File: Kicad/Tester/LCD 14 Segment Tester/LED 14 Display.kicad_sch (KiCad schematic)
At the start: 14 parts, among them IC4 SST39VF010-70-4I-WHE, IC5 SN74ABT245BDBR, IC8 SST39VF010-70-4I-WHE, IC9 SN74ABT245BDBR

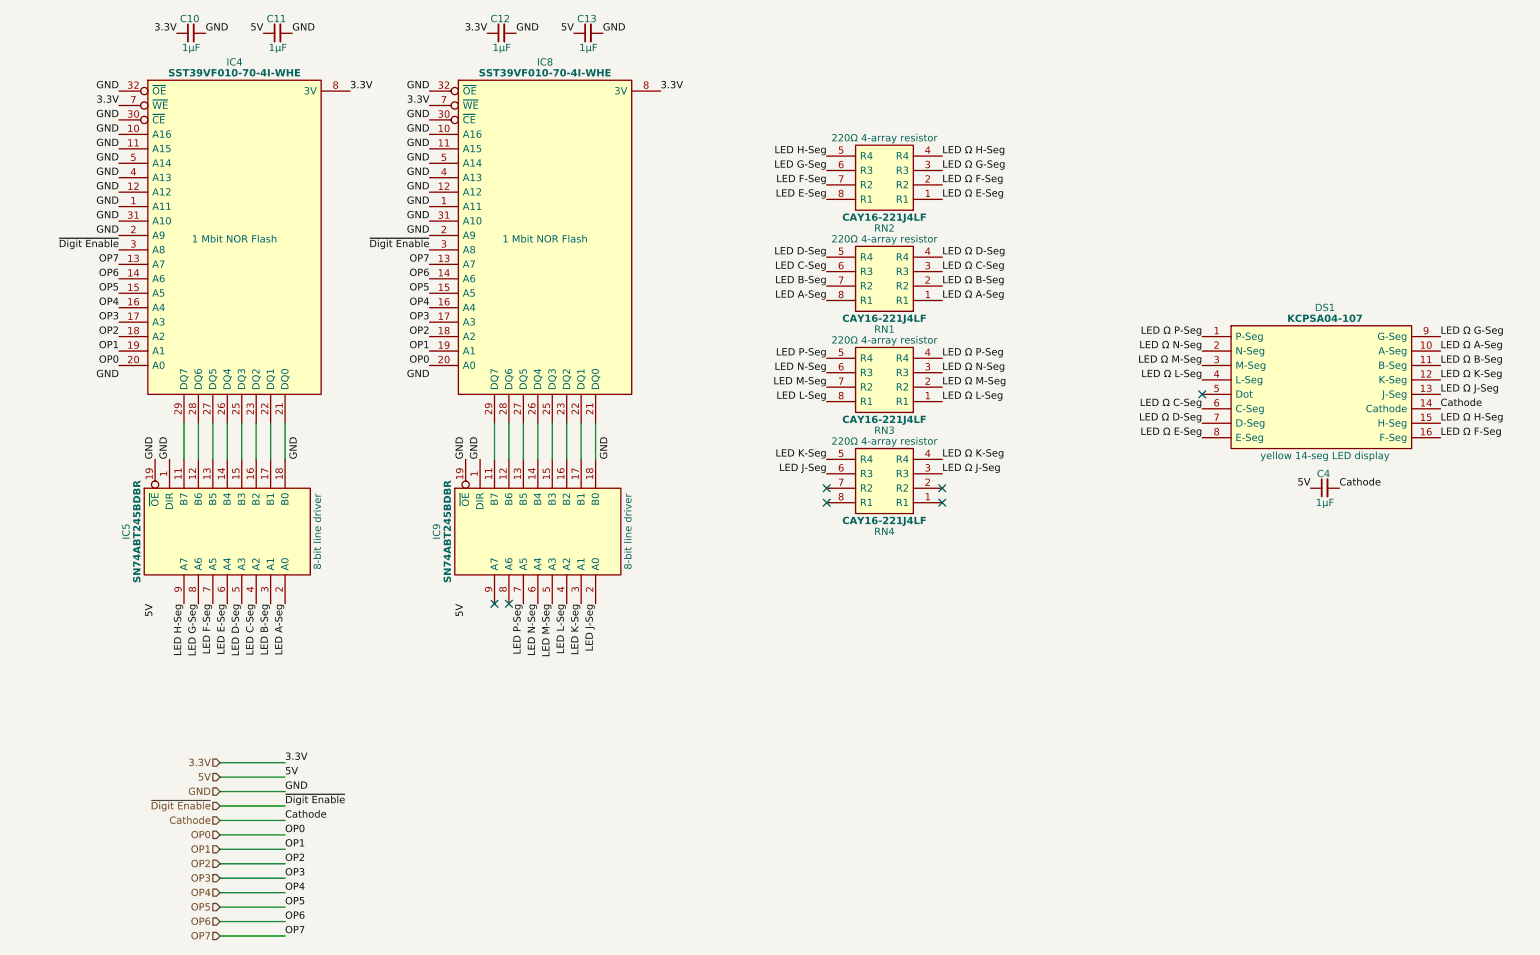
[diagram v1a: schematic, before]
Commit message: Laid out LCD 14 Segment tester PCB.
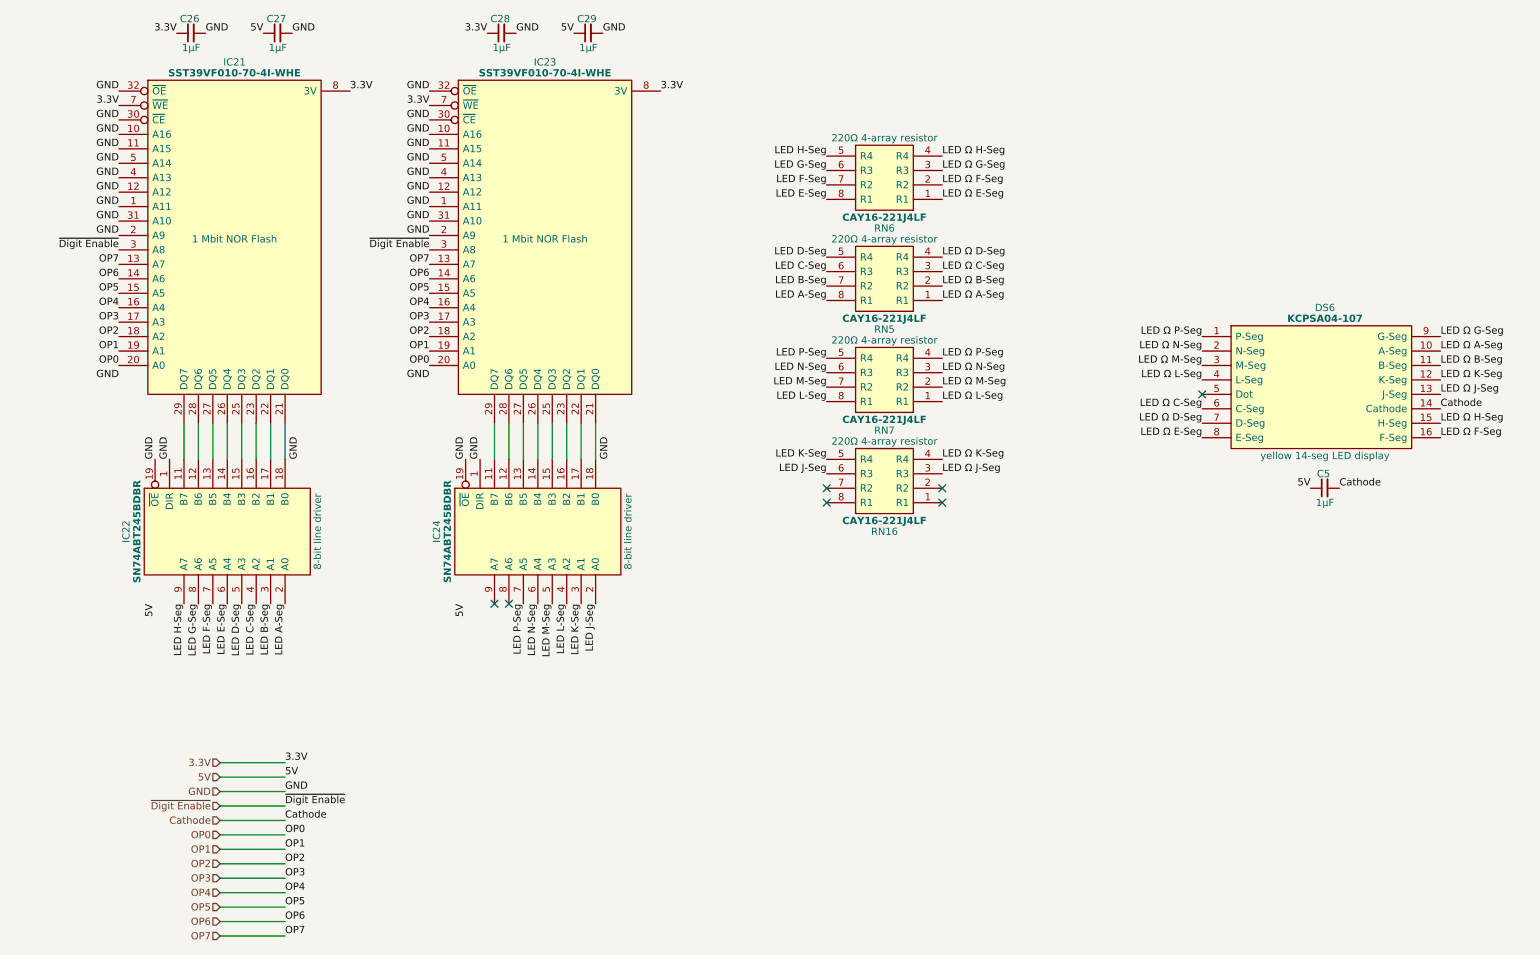
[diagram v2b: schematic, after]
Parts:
- IC21: renamed from IC4; footprint SamacSys_Parts:SOP50P1400X120-32N -> SamacSys_Parts:DIP-32_TSSOP_14mm_Adapter
- IC23: renamed from IC8; footprint SamacSys_Parts:SOP50P1400X120-32N -> SamacSys_Parts:DIP-32_TSSOP_14mm_Adapter
- renumbered C10 to C26, C11 to C27, C12 to C28, C13 to C29, C4 to C5, DS1 to DS6, IC5 to IC22, IC9 to IC24, RN4 to RN16, RN1 to RN5, RN2 to RN6, RN3 to RN7
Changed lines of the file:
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@@
 		(on_board yes)
 		(dnp no)
-		(property "Reference" "RN1"
+		(property "Reference" "RN5"
 			(at 160.02 82.55 0)
 			(effects
@@
 		(on_board yes)
 		(dnp no)
-		(property "Reference" "C12"
+		(property "Reference" "C28"
 			(at 92.456 27.94 0)
 			(effects
@@
 		(on_board yes)
 		(dnp no)
-		(property "Reference" "C13"
+		(property "Reference" "C29"
 			(at 107.696 27.94 0)
 			(effects
@@
 		(on_board yes)
 		(dnp no)
-		(property "Reference" "IC5"
+		(property "Reference" "IC22"
 			(at 26.67 118.11 0)
 			(effects
@@
 		(on_board yes)
 		(dnp no)
-		(property "Reference" "IC9"
+		(property "Reference" "IC24"
 			(at 81.28 118.11 0)
 			(effects
@@
 		(on_board yes)
 		(dnp no)
-		(property "Reference" "C10"
+		(property "Reference" "C26"
 			(at 37.846 27.94 0)
 			(effects
@@
 		(on_board yes)
 		(dnp no)
-		(property "Reference" "IC4"
+		(property "Reference" "IC21"
 			(at 45.72 35.56 0)
 			(effects
@@
 			)
 		)
-		(property "Footprint" "SamacSys_Parts:SOP50P1400X120-32N"
+		(property "Footprint" "SamacSys_Parts:DIP-32_TSSOP_14mm_Adapter"
 			(at 64.135 97.79 0)
 			(effects
@@
 		(on_board yes)
 		(dnp no)
-		(property "Reference" "DS1"
+		(property "Reference" "DS6"
 			(at 237.49 78.74 0)
 			(effects
@@
 		(on_board yes)
 		(dnp no)
-		(property "Reference" "RN4"
+		(property "Reference" "RN16"
 			(at 160.02 118.11 0)
 			(effects
@@
 		(on_board yes)
 		(dnp no)
-		(property "Reference" "C11"
+		(property "Reference" "C27"
 			(at 53.086 27.94 0)
 			(effects
@@
 		(on_board yes)
 		(dnp no)
-		(property "Reference" "RN2"
+		(property "Reference" "RN6"
 			(at 160.02 64.77 0)
 			(effects
@@
 		(on_board yes)
 		(dnp no)
-		(property "Reference" "IC8"
+		(property "Reference" "IC23"
 			(at 100.33 35.56 0)
 			(effects
@@
 			)
 		)
-		(property "Footprint" "SamacSys_Parts:SOP50P1400X120-32N"
+		(property "Footprint" "SamacSys_Parts:DIP-32_TSSOP_14mm_Adapter"
 			(at 118.745 97.79 0)
 			(effects
@@
 		(on_board yes)
 		(dnp no)
-		(property "Reference" "C4"
+		(property "Reference" "C5"
 			(at 237.236 107.95 0)
 			(effects
@@
 		(on_board yes)
 		(dnp no)
-		(property "Reference" "RN3"
+		(property "Reference" "RN7"
 			(at 160.02 100.33 0)
 			(effects
